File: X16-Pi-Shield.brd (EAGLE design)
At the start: 80 x 74.3 mm, 40 parts, among them J1 CONN_DF13-4P-1.25DSA, J3 CONN_DF13-4P-1.25DSA, J4 HTST-110-04-L-D-RA, J5 BM04B-GHS-TBT, J6 BM04B-GHS-TBT, U1 INA260AIPW, U2 AZ1117IH-3.3TRG1

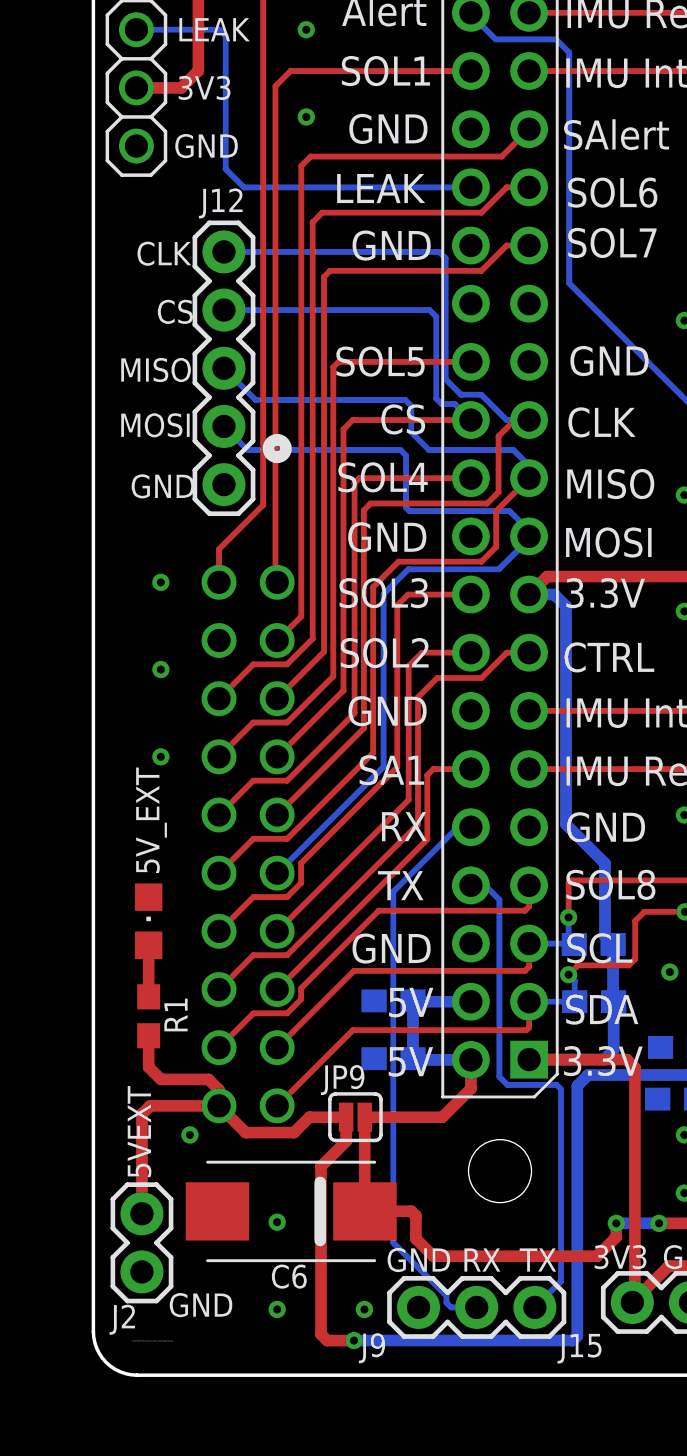
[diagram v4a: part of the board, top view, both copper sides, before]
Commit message: Revert "Minh Update 3"
This reverts commit ef018cd753ae75237427e996904381017dc6cda3.
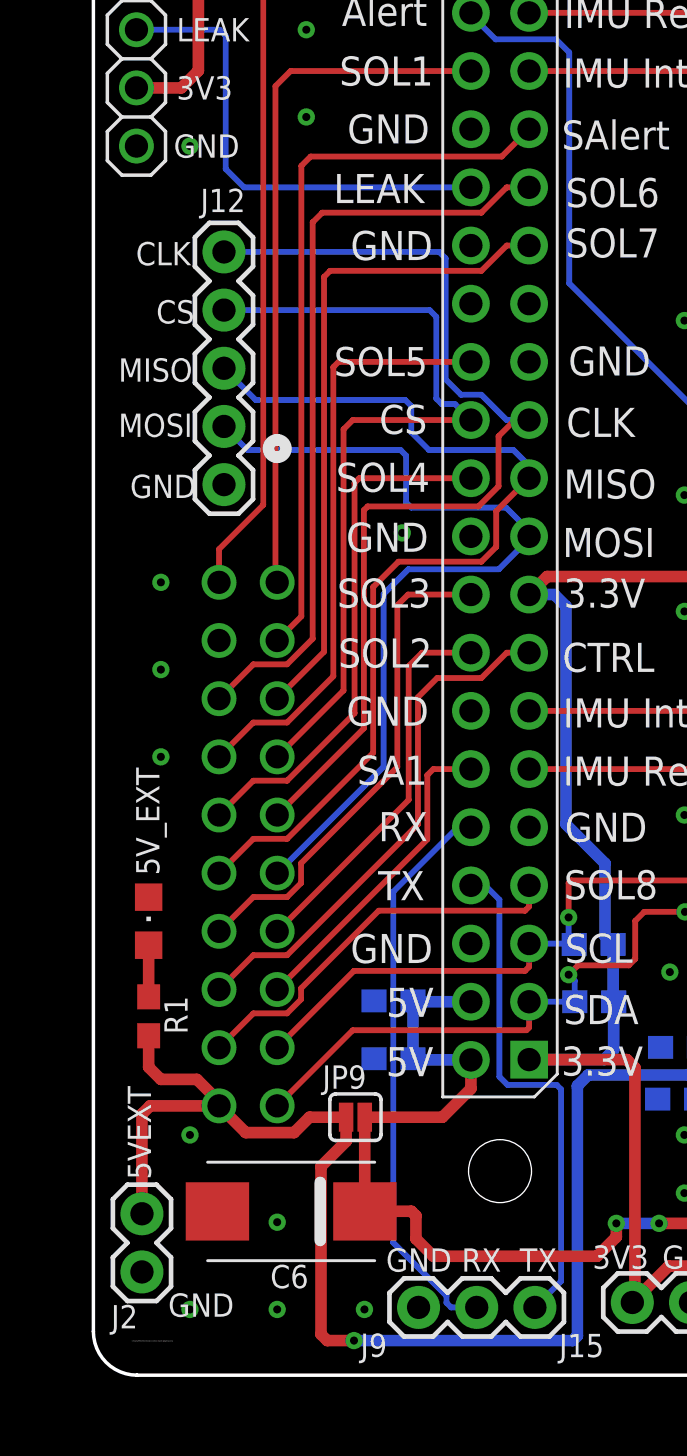
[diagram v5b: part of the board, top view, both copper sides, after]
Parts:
- R1, R15: value (none) -> 250
- R11, R12: value (none) -> 10k
- R16: value (none) -> 150
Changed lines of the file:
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@@
 <setting verticaltext="up"/>
 </settings>
-<grid distance="1" unitdist="mil" unit="mil" style="lines" multiple="1" display="yes" altdistance="5" altunitdist="mil" altunit="mil"/>
+<grid distance="50" unitdist="mil" unit="mil" style="lines" multiple="1" display="yes" altdistance="5" altunitdist="mil" altunit="mil"/>
 <layers>
 <layer number="1" name="Top" color="4" fill="1" visible="yes" active="yes"/>
@@
 <attribute name="VALUE" x="9.7663" y="10.8077" size="0.6096" layer="27" font="vector" ratio="20" rot="R180" align="top-center"/>
 </element>
-<element name="R11" library="SparkFun-Resistors" library_urn="urn:adsk.eagle:library:532" package="0603" package3d_urn="urn:adsk.eagle:package:39650/1" value=" " x="20.193" y="14.7066" smashed="yes" rot="MR180">
+<element name="R11" library="SparkFun-Resistors" library_urn="urn:adsk.eagle:library:532" package="0603" package3d_urn="urn:adsk.eagle:package:39650/1" value="10k" x="20.193" y="14.7066" smashed="yes" rot="MR180">
 <attribute name="NAME" x="22.987" y="14.7574" size="1.016" layer="26" font="vector" ratio="15" rot="MR0" align="bottom-center"/>
 <attribute name="PROD_ID" value=" " x="77.343" y="177.2666" size="1.778" layer="28" rot="MR180" display="off"/>
 <attribute name="VALUE" x="20.193" y="15.4686" size="0.6096" layer="28" font="vector" ratio="20" rot="MR180" align="top-center"/>
 </element>
-<element name="R12" library="SparkFun-Resistors" library_urn="urn:adsk.eagle:library:532" package="0603" package3d_urn="urn:adsk.eagle:package:39650/1" value=" " x="20.1676" y="17.2085" smashed="yes" rot="MR180">
+<element name="R12" library="SparkFun-Resistors" library_urn="urn:adsk.eagle:library:532" package="0603" package3d_urn="urn:adsk.eagle:package:39650/1" value="10k" x="20.1676" y="17.2085" smashed="yes" rot="MR180">
 <attribute name="NAME" x="23.1394" y="16.7005" size="1.016" layer="26" font="vector" ratio="15" rot="MR0" align="bottom-center"/>
 <attribute name="PROD_ID" value=" " x="81.1276" y="179.7685" size="1.778" layer="28" rot="MR180" display="off"/>
 <attribute name="VALUE" x="20.1676" y="17.9705" size="0.6096" layer="28" font="vector" ratio="20" rot="MR180" align="top-center"/>
 </element>
-<element name="R15" library="SparkFun-Resistors" library_urn="urn:adsk.eagle:library:532" package="0603" package3d_urn="urn:adsk.eagle:package:39650/1" value=" " x="26.5811" y="5.0292" smashed="yes" rot="R180">
+<element name="R15" library="SparkFun-Resistors" library_urn="urn:adsk.eagle:library:532" package="0603" package3d_urn="urn:adsk.eagle:package:39650/1" value="250" x="26.5811" y="5.0292" smashed="yes" rot="R180">
 <attribute name="NAME" x="26.5049" y="6.1468" size="1.016" layer="25" font="vector" ratio="15" align="bottom-center"/>
 <attribute name="PROD_ID" value=" " x="-38.1889" y="167.5892" size="1.778" layer="27" rot="R180" display="off"/>
 <attribute name="VALUE" x="26.5811" y="5.7912" size="0.6096" layer="27" font="vector" ratio="20" rot="R180" align="top-center"/>
 </element>
-<element name="R16" library="SparkFun-Resistors" library_urn="urn:adsk.eagle:library:532" package="0603" package3d_urn="urn:adsk.eagle:package:39650/1" value=" " x="37.465" y="9.271" smashed="yes" rot="R270">
+<element name="R16" library="SparkFun-Resistors" library_urn="urn:adsk.eagle:library:532" package="0603" package3d_urn="urn:adsk.eagle:package:39650/1" value="150" x="37.465" y="9.271" smashed="yes" rot="R270">
 <attribute name="NAME" x="36.322" y="9.271" size="1.016" layer="25" font="vector" ratio="15" rot="R90" align="bottom-center"/>
 <attribute name="PROD_ID" value=" " x="-125.095" y="-59.309" size="1.778" layer="27" rot="R270" display="off"/>
@@
 <attribute name="VALUE" x="0.7366" y="17.5895" size="0.6096" layer="27" font="vector" ratio="20" align="top-center"/>
 </element>
-<element name="R1" library="SparkFun-Resistors" library_urn="urn:adsk.eagle:library:532" package="0603" package3d_urn="urn:adsk.eagle:package:39650/1" value=" " x="0.7366" y="14.0716" smashed="yes" rot="R270">
+<element name="R1" library="SparkFun-Resistors" library_urn="urn:adsk.eagle:library:532" package="0603" package3d_urn="urn:adsk.eagle:package:39650/1" value="250" x="0.7366" y="14.0716" smashed="yes" rot="R270">
 <attribute name="NAME" x="2.4384" y="14.1224" size="1.016" layer="25" font="vector" ratio="15" rot="R90" align="bottom-center"/>
 <attribute name="PROD_ID" value=" " x="-1.8288" y="13.9192" size="1.778" layer="27" rot="R270" display="off"/>
@@
 <via x="10.16" y="1.27" extent="1-16" drill="0.35"/>
 <via x="6.35" y="1.27" extent="1-16" drill="0.35"/>
+<via x="2.54" y="1.27" extent="1-16" drill="0.35"/>
 <via x="6.35" y="5.08" extent="1-16" drill="0.35"/>
 <via x="2.54" y="8.89" extent="1-16" drill="0.35"/>
@@
 <via x="1.27" y="29.21" extent="1-16" drill="0.35"/>
 <via x="1.27" y="33.02" extent="1-16" drill="0.35"/>
+<via x="2.54" y="52.07" extent="1-16" drill="0.35"/>
 <via x="7.62" y="53.34" extent="1-16" drill="0.35"/>
 <via x="7.62" y="57.15" extent="1-16" drill="0.35"/>
@@
 <via x="1.27" y="62.23" extent="1-16" drill="0.35"/>
 <via x="4.572" y="59.69" extent="1-16" drill="0.35"/>
+<via x="11.811" y="35.179" extent="1-16" drill="0.35"/>
 </signal>
 <signal name="TX">
@@
 <wire x1="6.35" y1="22.86" x2="10.1346" y2="26.6446" width="0.254" layer="1"/>
 <wire x1="10.1346" y1="26.6446" x2="10.1346" y2="36.1696" width="0.254" layer="1"/>
-<wire x1="15.51986875" y1="36.4617" x2="16.0147" y2="36.95653125" width="0.254" layer="1"/>
-<wire x1="10.1346" y1="36.1696" x2="10.4267" y2="36.4617" width="0.254" layer="1"/>
-<wire x1="10.4267" y1="36.4617" x2="15.51986875" y2="36.4617" width="0.254" layer="1"/>
-<wire x1="16.0147" y1="36.95653125" x2="16.0147" y2="39.3954" width="0.254" layer="1"/>
+<wire x1="15.13886875" y1="36.3347" x2="16.0147" y2="37.21053125" width="0.254" layer="1"/>
+<wire x1="10.1346" y1="36.1696" x2="10.2997" y2="36.3347" width="0.254" layer="1"/>
+<wire x1="10.2997" y1="36.3347" x2="15.13886875" y2="36.3347" width="0.254" layer="1"/>
+<wire x1="16.0147" y1="37.21053125" x2="16.0147" y2="39.3954" width="0.254" layer="1"/>
 <wire x1="16.7259" y1="40.1066" x2="16.0147" y2="39.3954" width="0.254" layer="1"/>
 <wire x1="16.7259" y1="40.1066" x2="17.3482" y2="40.1066" width="0.254" layer="1"/>
@@
 <wire x1="4.0259" y1="39.8272" x2="5.0546" y2="38.7985" width="0.254" layer="16"/>
 <wire x1="11.7348" y1="38.7985" x2="11.9761" y2="38.5572" width="0.254" layer="16"/>
-<wire x1="11.9761" y1="38.5572" x2="11.9761" y2="36.2839" width="0.254" layer="16"/>
+<wire x1="11.9761" y1="38.5572" x2="11.9761" y2="36.5125" width="0.254" layer="16"/>
 <wire x1="17.3482" y1="35.2806" x2="17.3482" y2="35.0266" width="0.254" layer="16"/>
 <wire x1="5.0546" y1="38.7985" x2="11.7348" y2="38.7985" width="0.254" layer="16"/>
-<wire x1="16.4973" y1="36.1315" x2="17.3482" y2="35.2806" width="0.254" layer="16"/>
-<wire x1="11.9761" y1="36.2839" x2="12.1285" y2="36.1315" width="0.254" layer="16"/>
-<wire x1="12.1285" y1="36.1315" x2="16.4973" y2="36.1315" width="0.254" layer="16"/>
+<wire x1="16.3449" y1="36.2839" x2="17.3482" y2="35.2806" width="0.254" layer="16"/>
+<wire x1="11.9761" y1="36.5125" x2="12.2047" y2="36.2839" width="0.254" layer="16"/>
+<wire x1="12.2047" y1="36.2839" x2="16.3449" y2="36.2839" width="0.254" layer="16"/>
 </signal>
 <signal name="IMU_INT">
@@
 <contactref element="R1" pad="2"/>
 <wire x1="0.7366" y1="13.2216" x2="0.7366" y2="11.8491" width="0.508" layer="1"/>
-<wire x1="1.27" y1="11.3157" x2="3.3528" y2="11.3157" width="0.508" layer="1"/>
-<wire x1="3.3528" y1="11.3157" x2="3.81" y2="10.8585" width="0.508" layer="1"/>
-<wire x1="3.81" y1="10.8585" x2="3.81" y2="10.16" width="0.508" layer="1"/>
+<wire x1="1.27" y1="11.3157" x2="2.8448" y2="11.3157" width="0.508" layer="1"/>
+<wire x1="2.8448" y1="11.3157" x2="3.81" y2="10.3505" width="0.508" layer="1"/>
+<wire x1="3.81" y1="10.3505" x2="3.81" y2="10.16" width="0.508" layer="1"/>
 <wire x1="0.7366" y1="11.8491" x2="1.27" y2="11.3157" width="0.508" layer="1"/>
 <wire x1="9.3599" y1="9.6647" x2="9.3599" y2="8.6106" width="0.508" layer="1"/>

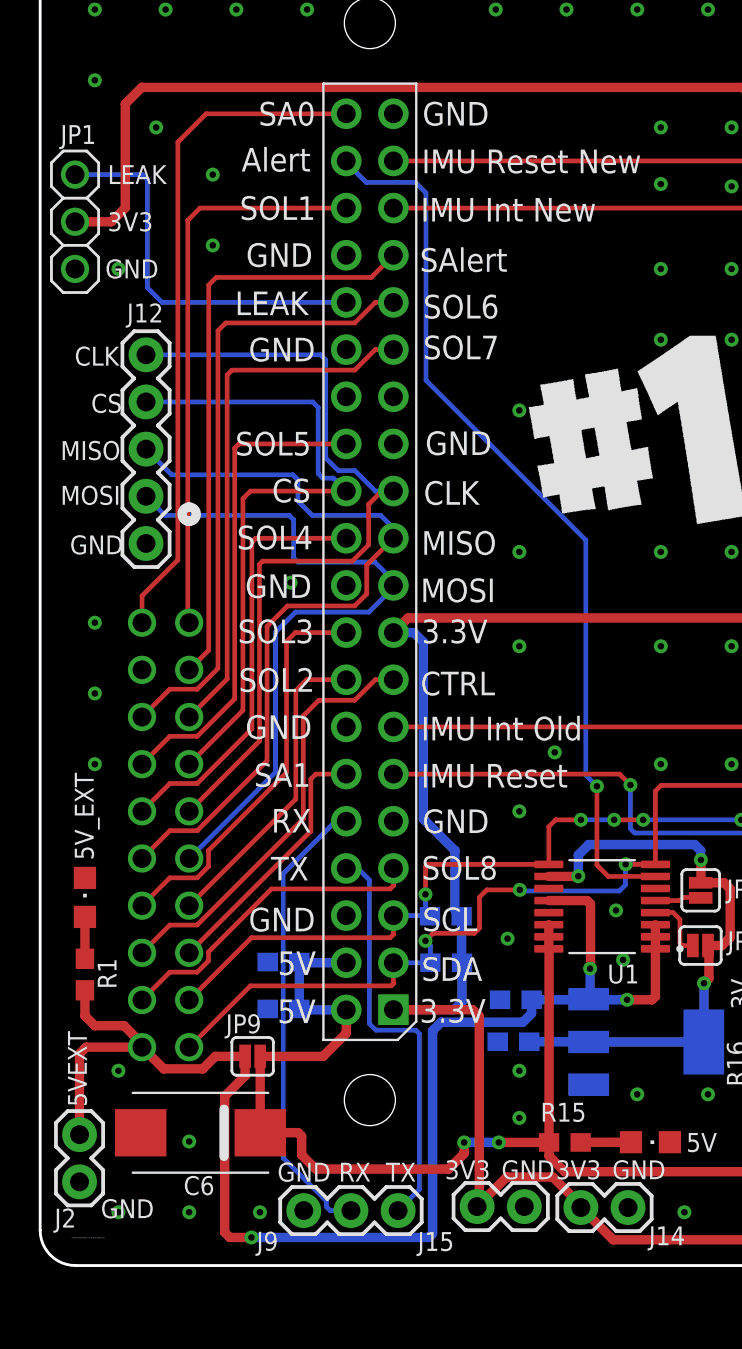
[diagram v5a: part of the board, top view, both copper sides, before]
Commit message: Minh Update 4 - Edit PMBUS traces, and modify Label + Traces
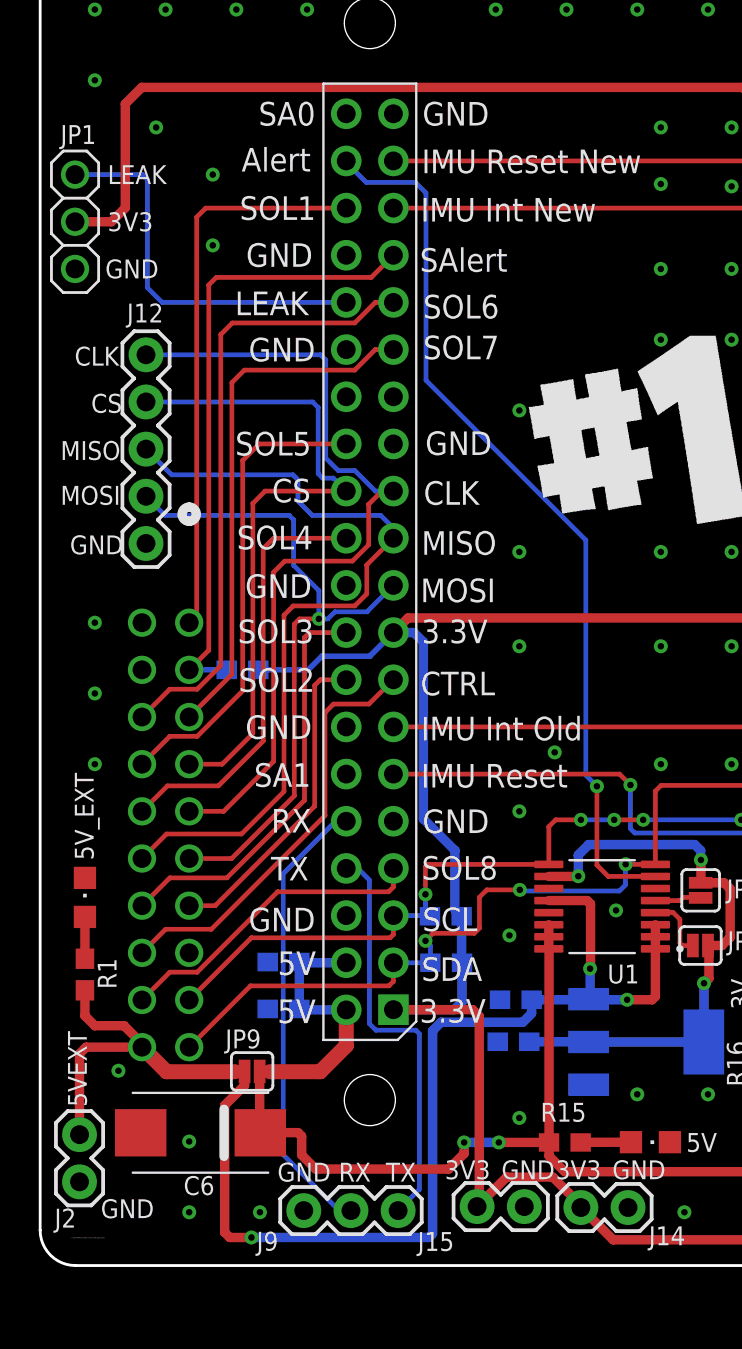
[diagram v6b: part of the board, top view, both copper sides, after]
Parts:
- added R2: 10k, SparkFun-Resistors:0603
- C4: value 2.2uF -> 10uF
- C5: value 2.2uF -> 22uF
- moved JP9 0.81 mm to (9.74, 8.85)
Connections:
- removed net SA0: J4.2, U$1.40
- removed net SA1: J4.15, U$1.12
- net 3V3: now also R2.2
- net SALERT: now also R2.1
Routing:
- net SA0: track 36.4 -> 0.00 mm
- net SA1: track 14.1 -> 0.00 mm
- net 3V3: track 286.2 -> 294.3 mm
- net SALERT: track 31.8 -> 33.8 mm
- net MOSI: track 38.2 -> 36.9 mm, vias 0 -> 1
- net MISO: track 42.1 -> 43.5 mm
- net 5V_EXT: track 76.3 -> 75.2 mm
- net GPIO_5: track 26.0 -> 25.4 mm
- net CS: track 36.1 -> 36.7 mm

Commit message: Minh Update 5
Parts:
- moved R2 0.18 mm to (9.40, 30.5)
- renumbered 3V to 3V_LED, 5V to 5V_LED
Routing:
- net GND: track 0.00 -> 6.72 mm, vias 151 -> 152
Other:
- board text added: "X16 Pi ShieldSahil Mitra; Leads: Danial, Minh, Raghav, Vijay"
- board text removed: "X16 Pi Shield; By Sahil Mitra; Leads: Danial, Minh, Raghav, Vijay"
